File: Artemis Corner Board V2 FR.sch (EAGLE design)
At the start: 64 parts, among them U1 TPS562219, U2 TM4C1231C3PM, U21 LM1085IS, U3 TPS562219, U4 MCP2562FD

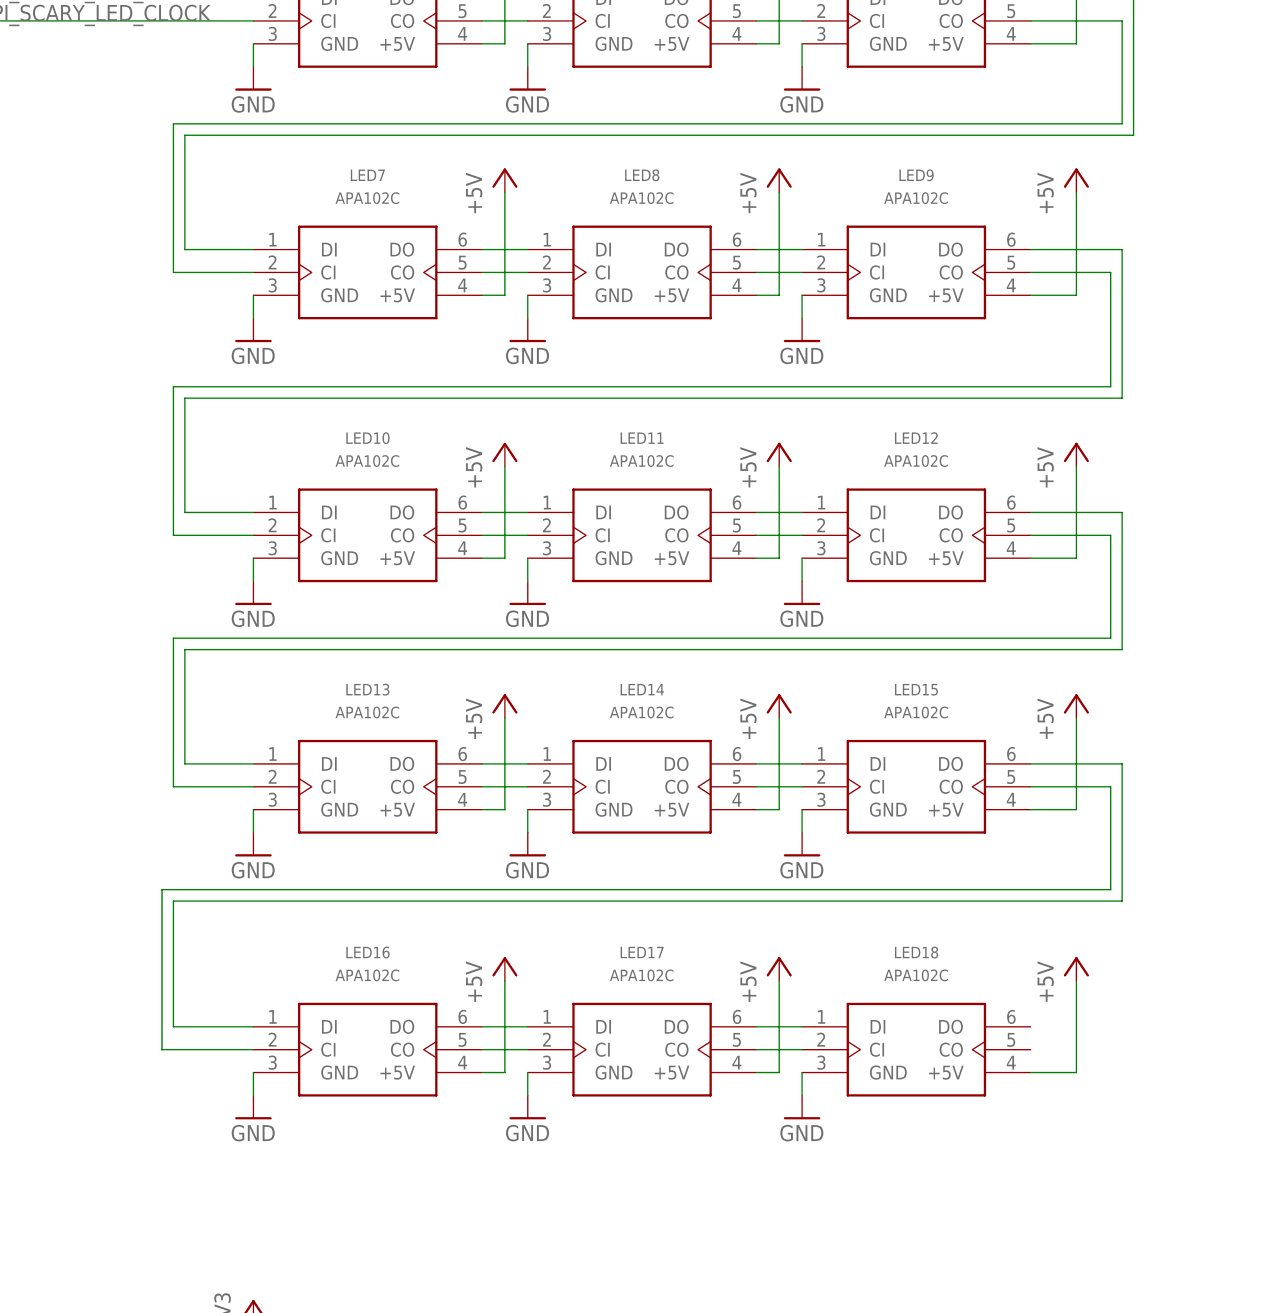
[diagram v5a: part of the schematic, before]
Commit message: Down to only 4 LEDs
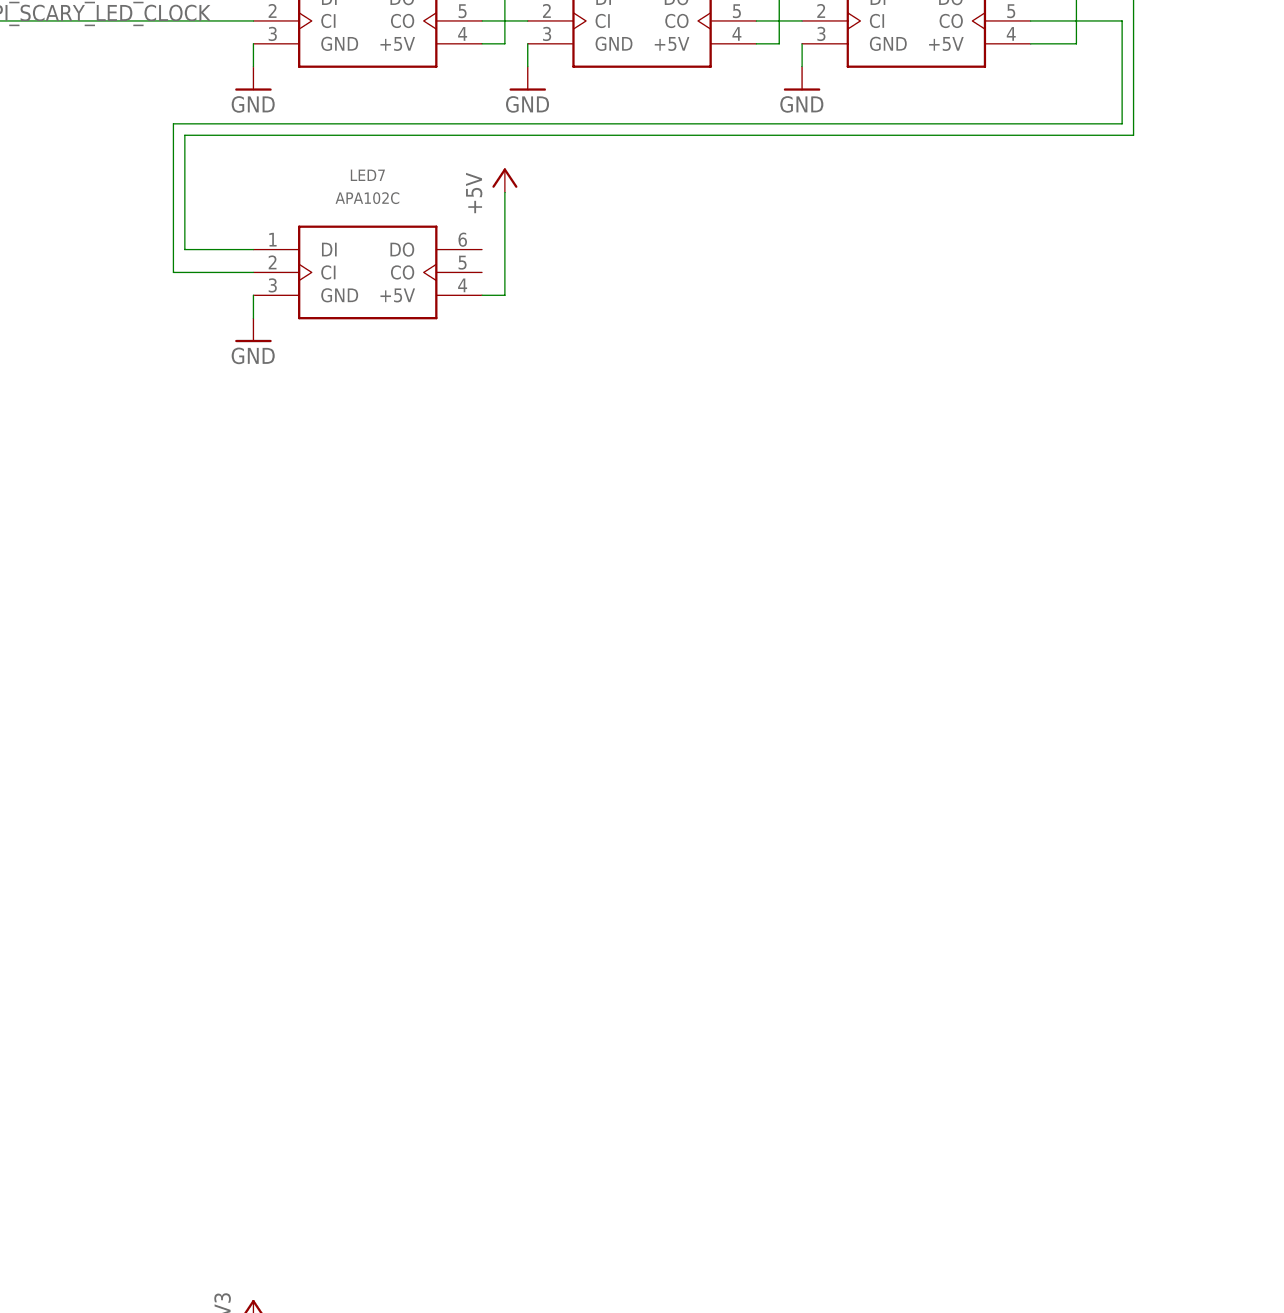
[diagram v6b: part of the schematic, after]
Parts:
- removed LED10, LED11, LED12, LED13, LED14, LED15, LED16, LED17, LED18, LED8, LED9: APA102C, FormE:APA102C
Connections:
- removed net N$14: LED10.DO, LED11.DI
- removed net N$19: LED11.DO, LED12.DI
- removed net N$20: LED11.CO, LED12.CI
- removed net N$21: LED10.CO, LED11.CI
- removed net N$22: LED10.DI, LED9.DO
- removed net N$23: LED10.CI, LED9.CO
- removed net N$24: LED13.DO, LED14.DI
- removed net N$25: LED14.DO, LED15.DI
- removed net N$26: LED14.CO, LED15.CI
- removed net N$27: LED13.CO, LED14.CI
- removed net N$28: LED12.DO, LED13.DI
- removed net N$29: LED12.CO, LED13.CI
- removed net N$30: LED16.DO, LED17.DI
- removed net N$31: LED17.DO, LED18.DI
- removed net N$32: LED17.CO, LED18.CI
- removed net N$33: LED16.CO, LED17.CI
- removed net N$34: LED15.CO, LED16.CI
- removed net N$35: LED15.DO, LED16.DI
- removed net N$5: LED7.DO, LED8.DI
- removed net N$6: LED8.DO, LED9.DI
- removed net N$7: LED8.CO, LED9.CI
- removed net N$8: LED7.CO, LED8.CI
- net +5V: no longer LED10.+5V, LED11.+5V, LED12.+5V, LED13.+5V, LED14.+5V, LED15.+5V, LED16.+5V, LED17.+5V, LED18.+5V, LED8.+5V, LED9.+5V
- net GND: no longer LED10.GND, LED11.GND, LED12.GND, LED13.GND, LED14.GND, LED15.GND, LED16.GND, LED17.GND, LED18.GND, LED8.GND, LED9.GND

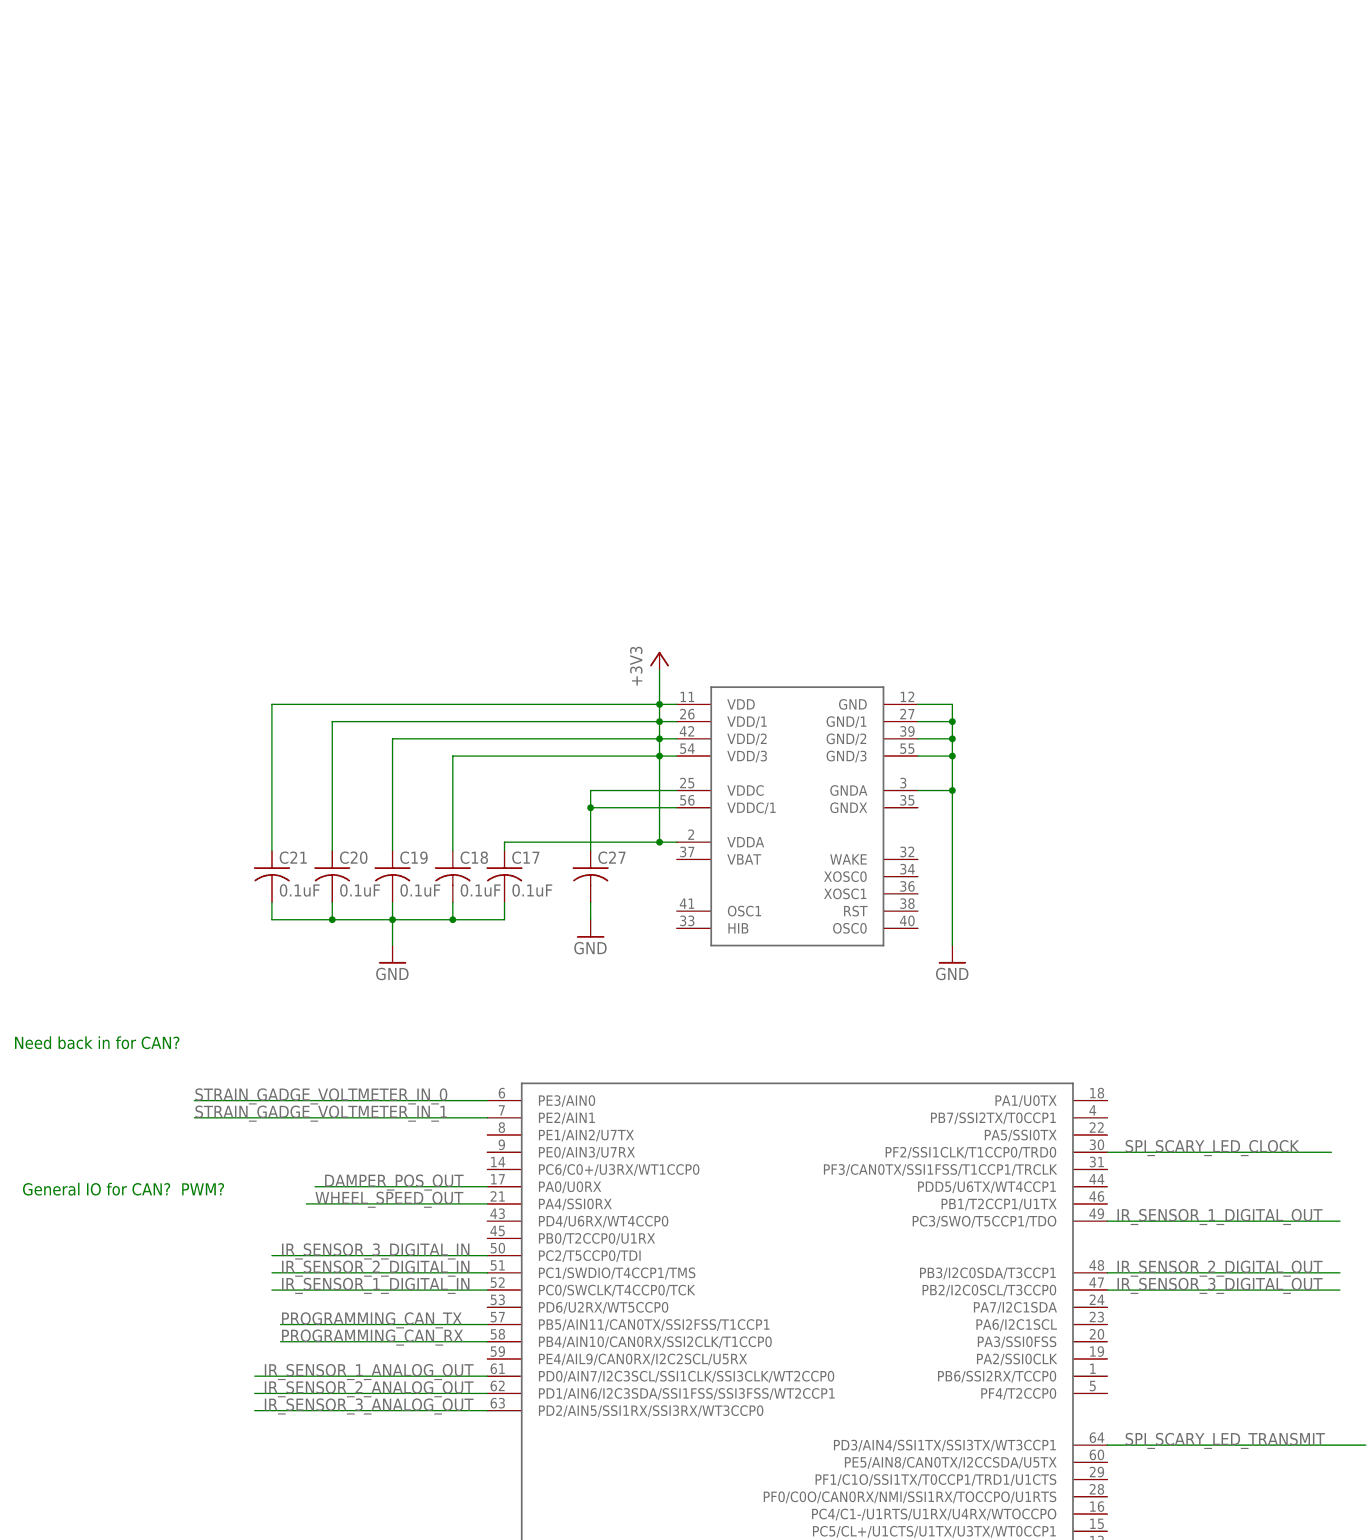
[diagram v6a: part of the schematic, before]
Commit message: Added decoupling CAPS and Button for reset
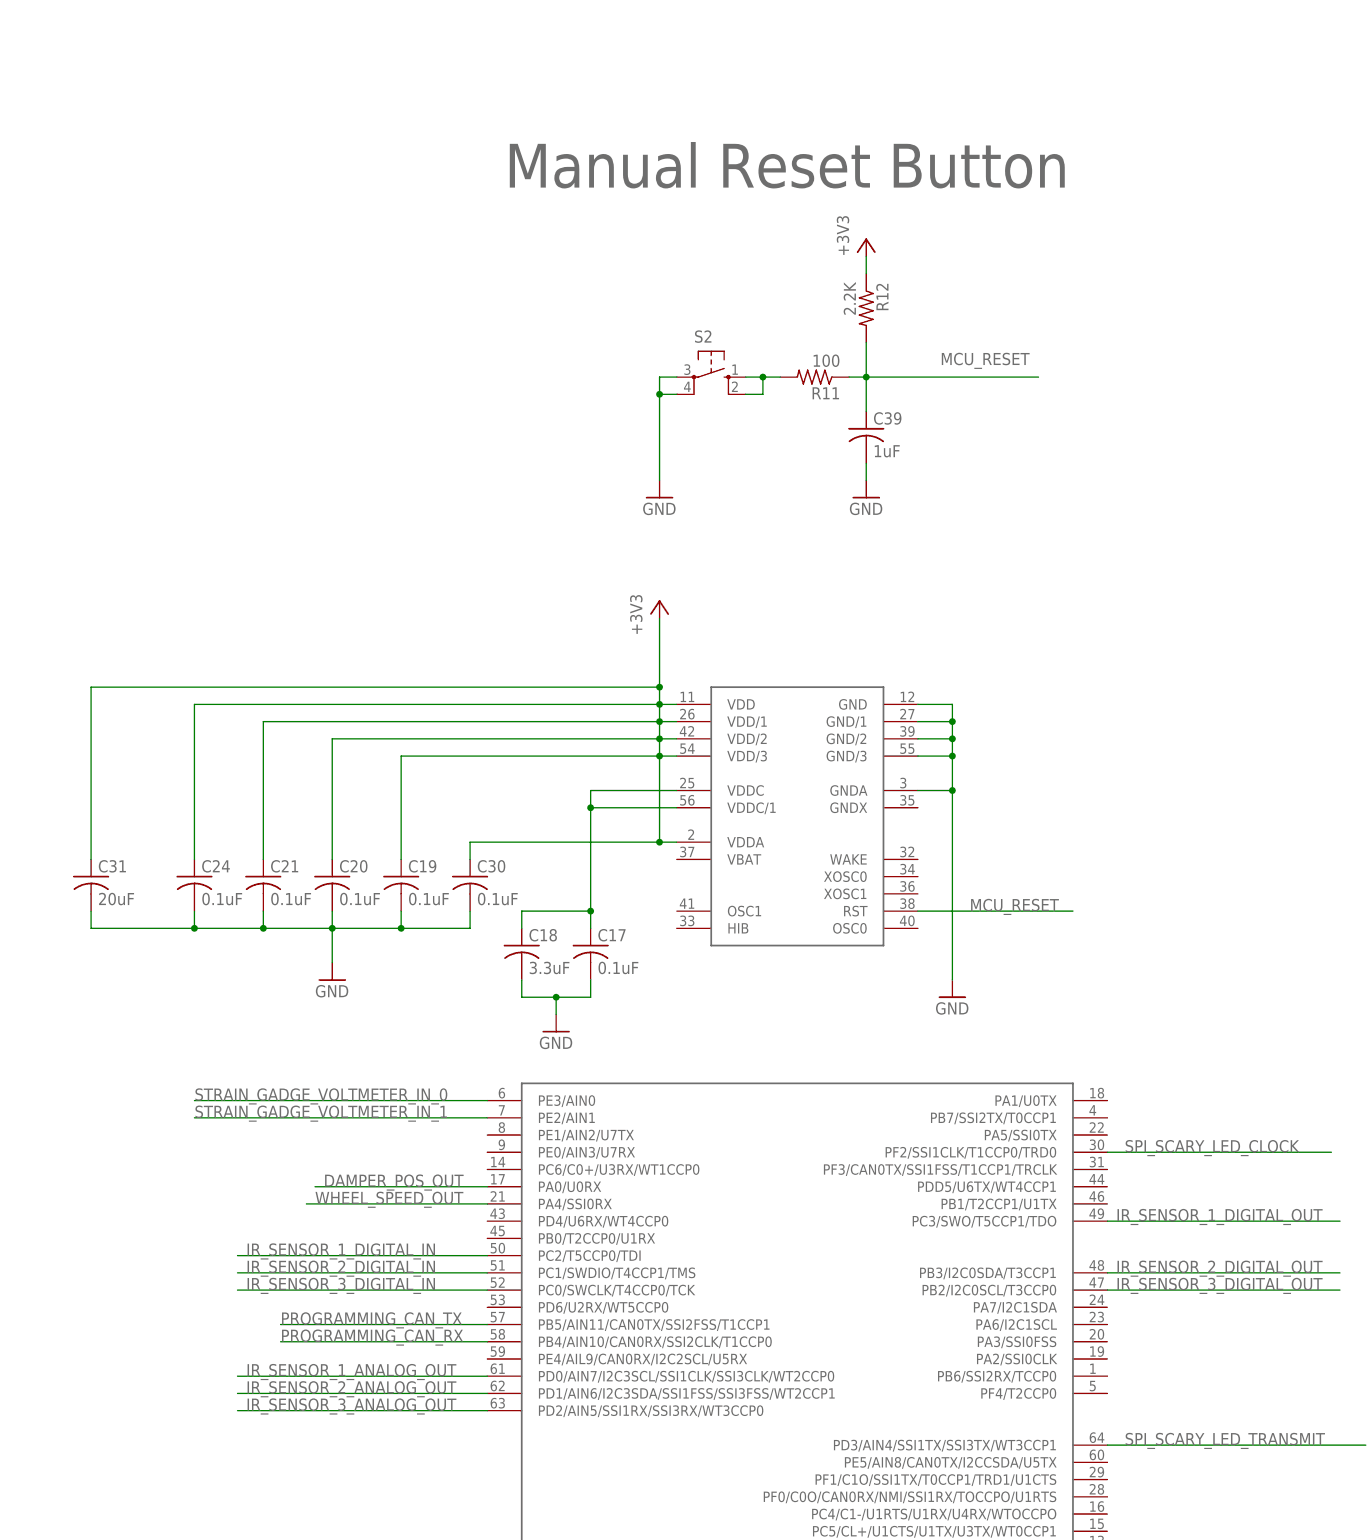
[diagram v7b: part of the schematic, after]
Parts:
- removed C27: 3.3uF, rcl:C-USC0805
- added C24, C30: 0.1uF, rcl:C-USC0805
- added C31: 20uF, rcl:C-USC0805
- added C39: 1uF, rcl:C-USC0805
- added R11: 100, rcl:R-US_R0805
- added R12: 2.2K, rcl:R-US_R0805
- added S2: TE-FSM4JSMATR, FormE:TE-FSM4JSMATR
- C17, C19, C20, C21: PARTNO GRM21BR71H104KA01L -> (none)
- C18: value 0.1uF -> 3.3uF; PARTNO GRM21BR71H104KA01L -> (none)
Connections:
- new net MCU_RESET: C39.1, R11.1, R12.2, U2.RST
- new net N$18: R11.2, S2.1, S2.2
- net +3V3: now also C24.1, C30.1, C31.1, R12.1; no longer C17.1, C18.1
- net GND: now also C24.2, C30.2, C31.2, C39.2, S2.3, S2.4; no longer C27.2
- net IR_SENSOR_1_DIGITAL_IN: now also U2.PC2/T5CCP0/TDI; no longer U2.PC0/SWCLK/T4CCP0/TCK
- net IR_SENSOR_3_DIGITAL_IN: now also U2.PC0/SWCLK/T4CCP0/TCK; no longer U2.PC2/T5CCP0/TDI
- net P$40: now also C17.1, C18.1; no longer C27.1
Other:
- note added: "Manual Reset Button"
- note removed: "Need back in for CAN?"
- moved on the sheet: C17, C18, C19, C20, C21

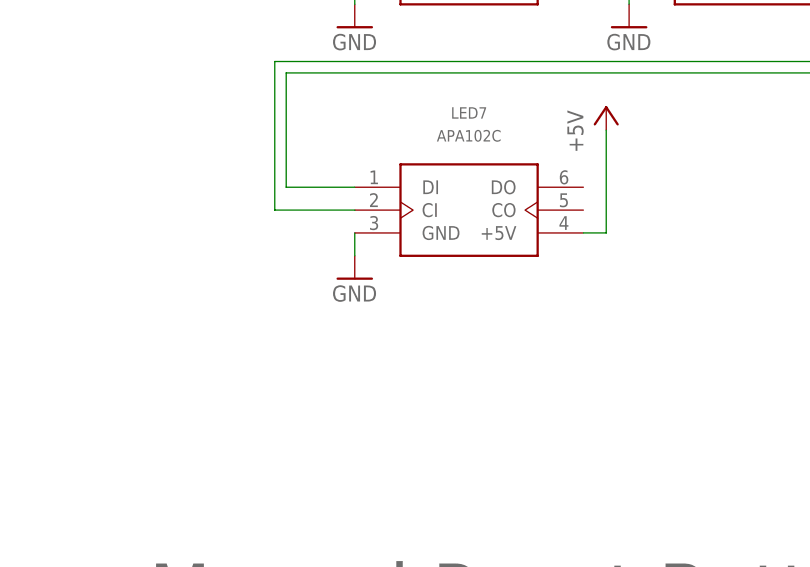
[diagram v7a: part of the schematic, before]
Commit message: About to go from IR sensors to Image sensor
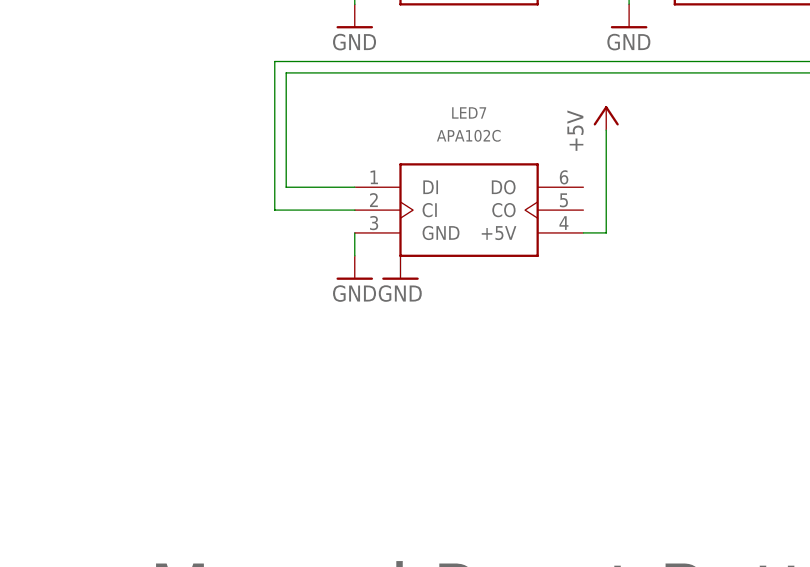
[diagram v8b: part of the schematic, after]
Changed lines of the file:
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@@
 <part name="C21" library="rcl" deviceset="C-US" device="C0805" value="0.1uF"/>
 <part name="C24" library="rcl" deviceset="C-US" device="C0805" value="0.1uF"/>
+<part name="GND1" library="supply1" deviceset="GND" device=""/>
 </parts>
 <sheets>
@@
 <instance part="C21" gate="G$1" x="-10.16" y="139.7"/>
 <instance part="C24" gate="G$1" x="-20.32" y="139.7"/>
+<instance part="GND1" gate="1" x="53.34" y="279.4"/>
 </instances>
 <busses>
